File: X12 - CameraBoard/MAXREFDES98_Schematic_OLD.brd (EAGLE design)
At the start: 87.8 x 25.4 mm, 32 parts, among them U1 MB110S-TP, U2 MB110S-TP, U3 MAX5969AETB+

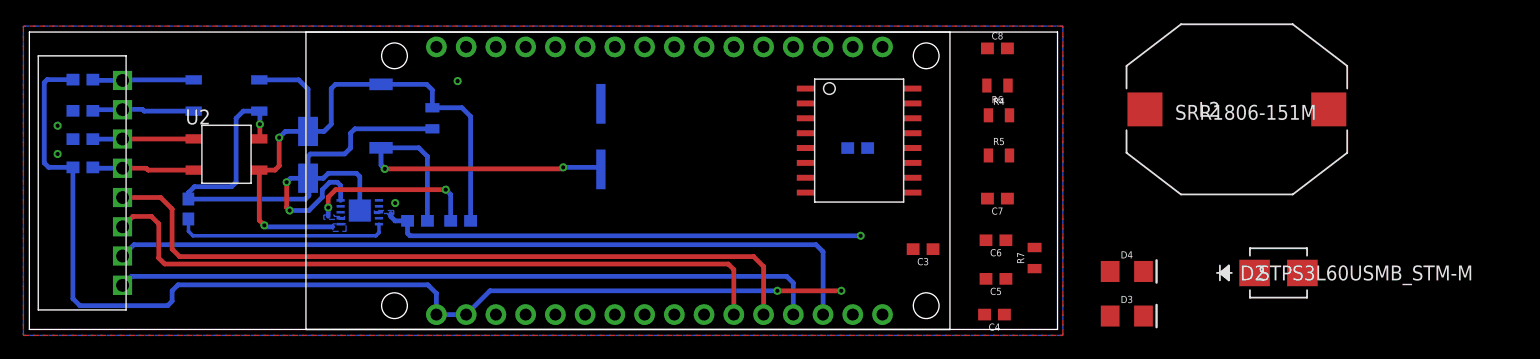
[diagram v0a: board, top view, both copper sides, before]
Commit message: Added new buck converter, plus supporting circuitry
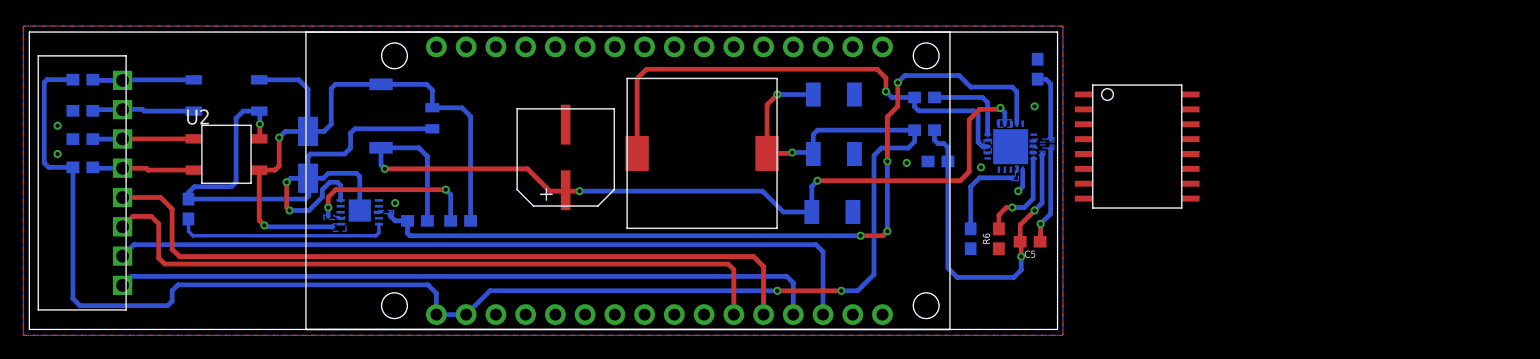
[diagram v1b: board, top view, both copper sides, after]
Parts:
- removed C3: 330uF, SparkFun-Capacitors:0603
- removed D2: STPS3L60USMB_STM-M, Camera_Board_Parts_09_30_2020:SMB_STM-M
- removed D3, D4: (no value), SparkFun-LED:FKIT-LED-1206
- removed R7: 20k, SparkFun-Resistors:0805
- added C10: 22uF, SparkFun-Capacitors:1210
- added U4: MAX17503ATP+, MAX17503ATP+:MAX17503ATP+
- C4: value 220uF -> 22uF; device SparkFun-Capacitors:0603 -> SparkFun-Capacitors:1210
- C5: value 220nF -> 1pF
- C6: value 2.7nF -> 0.018uF
- C7: value 22nF -> 2.2uF; device SparkFun-Capacitors:0603 -> SparkFun-Capacitors:1210
- C8: value 100nF -> 2.2uF
- C9: value 100nF -> 0.1uF
- L2: value SRR1806-151M -> SLF12575T-150M4R7-PF; device Camera_Board_Parts_09_30_2020:IND_BOURNS_SRR1806 -> SLF12575T-150M4R7-PF:SLF12575T-150M4R7-PF
- R4: value 2.7k -> 154k; device SparkFun-Resistors:0805 -> SparkFun-Resistors:0603
- R5: value 9.1k -> 34k; device SparkFun-Resistors:0805 -> SparkFun-Resistors:0603
- R6: value 4.7k -> 68k; device SparkFun-Resistors:0805 -> SparkFun-Resistors:0603
- moved L2 53.1 mm to (51.1, 8.64)
- moved U$1 23.8 mm to (94.6, 15.6)
- moved C4 19.4 mm to (68.7, 15.0), flipped to the bottom
- moved C8 16.4 mm to (80.4, 7.75), flipped to the bottom, turned to 270 degrees
- moved C6 15.0 mm to (86.1, 22.2), flipped to the bottom, turned to 90 degrees
- moved C7 14.1 mm to (68.6, 10.0), flipped to the bottom
- moved R6 13.1 mm to (82.8, 7.75), turned to 90 degrees
- moved C2 11.4 mm to (41.7, 10.5), flipped to the top
- moved C9 7.16 mm to (76.5, 19.8)
- moved R4 6.48 mm to (76.5, 17.0), flipped to the bottom
- moved R5 5.23 mm to (77.6, 14.4), flipped to the bottom, turned to 180 degrees
- moved C5 4.31 mm to (85.5, 7.49)
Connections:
- removed net BOOT: C9.1, U$1.12
- removed net COMP: R5.1, U$1.13
- removed net IND_IN: C9.2, D2.1, L2.2, U$1.5
- removed net LNK: D3.A, U$2.LNK
- removed net N$6: C7.1, R5.2
- removed net OSC: C6.1, R7.2, U$1.4
- removed net SPD: D4.A, U$2.SPD
- removed net SS_INH: C8.1, U$1.3
- new net BST: C9.1, U4.BST
- new net CF: C5.1, U4.CF
- new net EPAD: U4.EPAD
- new net LX: C9.2, L2.P$1, U4.LX1, U4.LX2, U4.LX3
- new net RESET: U4.*RESET
- new net RT: R6.2, U4.RT
- new net SS: C6.1, U4.SS
- new net VCC: C8.1, U4.VCC
- new net VIN: C2.PLUS, C7.1, L1.P$2, R3.2, U4.VIN1, U4.VIN2, U4.VIN3
- net 5V_OUT: now also C10.1, C4.1, L2.P$2; no longer C3.1, L2.1
- net FB: now also C5.2, R5.2, U4.FB; no longer R6.2, U$1.14
- net GND: now also C10.2, R5.1, U4.MODE, U4.PGND1, U4.PGND2, U4.PGND3, U4.SGND, U4.SYNC; no longer C3.2, C5.2, D2.2, D3.C, D4.C
- net PG_EN/UVLO: now also U4.EN/UVLO
- net VDD: no longer C2.PLUS, C4.1, C5.1, L1.P$2, R3.2, R7.1, U$1.11
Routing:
- net VIN: track 0.00 -> 75.0 mm, vias 0 -> 4
- net LX: track 0.00 -> 41.9 mm, vias 0 -> 1
- net 5V_OUT: track 93.3 -> 134.8 mm, vias 2 -> 4
- net VDD: track 84.4 -> 54.1 mm, vias 4 -> 2
- net FB: track 0.00 -> 30.1 mm, vias 0 -> 2
- net PG_EN/UVLO: track 41.7 -> 70.9 mm, vias 1 -> 4
- net CF: track 0.00 -> 8.37 mm, vias 0 -> 1
- net RT: track 0.00 -> 8.13 mm, vias 0 -> 1
- net VCC: track 0.00 -> 7.47 mm
- net BST: track 0.00 -> 7.46 mm
- net SS: track 0.00 -> 5.99 mm
- net GND: track 0.00 -> 1.99 mm, vias 4 -> 7
- added copper zone on layer 16, net CF
- added copper zone on layer 16, net FB
- added copper zone on layer 16, net LX
- added copper zone on layer 16, net SS
- added copper zone on layer 16, net VCC
- added copper zone on layer 16, net VIN
